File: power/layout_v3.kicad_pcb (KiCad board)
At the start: 2 copper layers, 38.1 x 58.4 mm, 11 parts

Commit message: Minor changes after first combine
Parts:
- removed REF** (x2): PinHeader_1x20_P2.54mm_Vertical, Connector_PinHeader_2.54mm:PinHeader_1x20_P2.54mm_Vertical
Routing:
- net VDD: track 62.3 -> 70.4 mm
- net +5V: track 33.3 -> 37.3 mm
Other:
- board outline removed

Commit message: WIP STM32{F,L}xxxCxTx layout
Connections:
- net +5V renamed 5V
- PD3 pad 2: (no net) -> VBAT
- PJ1 pad 4: (no net) -> Net-(PJ1-Pad4)
- PSJ1 pad 2: (no net) -> USB_D+
- PSJ2 pad 2: (no net) -> USB_D-
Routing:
- net +5V: track 0.00 -> 31.2 mm
- net 5V: track 37.3 -> 6.10 mm
- net VBAT: track 0.00 -> 16.3 mm
- net (no net): track 16.3 -> 0.00 mm
- net Net-(PJ1-Pad4): track 0.00 -> 11.5 mm
- net Net-(PJ1-Pad2): track 5.99 -> 5.27 mm
- net Net-(PJ1-Pad3): track 4.56 -> 5.27 mm
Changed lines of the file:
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@@
     (thickness 1.6)
     (drawings 16)
-    (tracks 56)
+    (tracks 61)
     (zones 0)
     (modules 9)
-    (nets 8)
+    (nets 13)
   )
   (page A4)
@@
   (net 6 "Net-(PJ1-Pad2)")
   (net 7 +5V)
+  (net 8 5V)
+  (net 9 VBAT)
+  (net 10 "Net-(PJ1-Pad4)")
+  (net 11 USB_D+)
+  (net 12 USB_D-)
   (net_class Default "Dit is de standaard class."
     (clearance 0.2)
@@
     (uvia_drill 0.1)
     (add_net +5V)
+    (add_net 5V)
     (add_net GND)
     (add_net "Net-(PJ1-Pad2)")
     (add_net "Net-(PJ1-Pad3)")
+    (add_net "Net-(PJ1-Pad4)")
+    (add_net USB_D+)
+    (add_net USB_D-)
+    (add_net VBAT)
     (add_net VBUS)
     (add_net VDD)
@@
       ))
     (pad 2 smd custom (at 0.65 0 270) (size 1 0.5) (layers B.Cu B.Mask)
-      (zone_connect 2)
+      (net 12 USB_D-) (zone_connect 2)
       (options (clearance outline) (anchor rect))
       (primitives
@@
       ))
     (pad 2 smd custom (at 0.65 0 270) (size 1 0.5) (layers B.Cu B.Mask)
-      (zone_connect 2)
+      (net 11 USB_D+) (zone_connect 2)
       (options (clearance outline) (anchor rect))
       (primitives
@@
     (pad 5 smd rect (at 1.3 -1.9 180) (size 0.45 1.3) (layers F.Cu F.Paste F.Mask)
       (net 1 GND))
-    (pad 4 smd rect (at 0.65 -1.9 180) (size 0.45 1.3) (layers F.Cu F.Paste F.Mask))
+    (pad 4 smd rect (at 0.65 -1.9 180) (size 0.45 1.3) (layers F.Cu F.Paste F.Mask)
+      (net 10 "Net-(PJ1-Pad4)"))
     (pad 3 smd rect (at 0 -1.9 180) (size 0.45 1.3) (layers F.Cu F.Paste F.Mask)
       (net 5 "Net-(PJ1-Pad3)"))
@@
     (fp_line (start -0.7 -0.6) (end -1 -0.3) (layer F.Fab) (width 0.1))
     (fp_line (start 1 -0.6) (end -0.7 -0.6) (layer F.Fab) (width 0.1))
-    (pad 2 smd roundrect (at 1.025 0) (size 1.15 1.4) (layers F.Cu F.Paste F.Mask) (roundrect_rratio 0.217391))
+    (pad 2 smd roundrect (at 1.025 0) (size 1.15 1.4) (layers F.Cu F.Paste F.Mask) (roundrect_rratio 0.217391)
+      (net 9 VBAT))
     (pad 1 smd roundrect (at -1.025 0) (size 1.15 1.4) (layers F.Cu F.Paste F.Mask) (roundrect_rratio 0.217391)
       (net 2 VREG_IN))
@@
       (net 4 VBUS))
     (pad 1 smd roundrect (at -1.025 0) (size 1.15 1.4) (layers F.Cu F.Paste F.Mask) (roundrect_rratio 0.217391)
-      (net 7 +5V))
+      (net 8 5V))
     (model ${KISYS3DMOD}/Diode_SMD.3dshapes/D_0805_2012Metric.wrl
       (at (xyz 0 0 0))
@@
   (gr_line (start 132.08 109.22) (end 170.18 109.22) (layer Dwgs.User) (width 0.05))
   (gr_line (start 132.08 50.8) (end 132.08 109.22) (layer Dwgs.User) (width 0.05))
-  (segment (start 162.56 60.96) (end 162.56 63.5) (width 0.25) (layer F.Cu) (net 0))
-  (segment (start 150.64 63.5) (end 149.37 62.23) (width 0.25) (layer F.Cu) (net 0))
-  (segment (start 162.56 63.5) (end 150.64 63.5) (width 0.25) (layer F.Cu) (net 0))
+  (segment (start 162.56 60.96) (end 162.56 63.5) (width 0.25) (layer F.Cu) (net 9))
+  (segment (start 150.64 63.5) (end 149.37 62.23) (width 0.25) (layer F.Cu) (net 9))
+  (segment (start 162.56 63.5) (end 150.64 63.5) (width 0.25) (layer F.Cu) (net 9))
   (via (at 143.256 70.104) (size 0.8) (drill 0.4) (layers F.Cu B.Cu) (net 1))
   (segment (start 145.025 69.85) (end 143.51 69.85) (width 0.25) (layer F.Cu) (net 1))
@@
   (segment (start 146.08 60.93) (end 146.08 56.51) (width 0.25) (layer F.Cu) (net 4))
   (segment (start 144.78 62.23) (end 146.08 60.93) (width 0.25) (layer F.Cu) (net 4))
-  (via (at 143.51 58.42) (size 0.8) (drill 0.4) (layers F.Cu B.Cu) (net 5))
-  (segment (start 142.24 59.69) (end 143.51 58.42) (width 0.25) (layer B.Cu) (net 5))
-  (segment (start 144.78 57.41) (end 144.78 56.51) (width 0.25) (layer F.Cu) (net 5))
-  (segment (start 144.075685 58.42) (end 144.78 57.715685) (width 0.25) (layer F.Cu) (net 5))
-  (segment (start 144.78 57.715685) (end 144.78 57.41) (width 0.25) (layer F.Cu) (net 5))
-  (segment (start 143.51 58.42) (end 144.075685 58.42) (width 0.25) (layer F.Cu) (net 5))
-  (via (at 144.78 59.69) (size 0.8) (drill 0.4) (layers F.Cu B.Cu) (net 6))
-  (segment (start 145.43 56.51) (end 145.43 59.04) (width 0.25) (layer F.Cu) (net 6))
-  (segment (start 145.43 59.04) (end 144.78 59.69) (width 0.25) (layer F.Cu) (net 6))
-  (segment (start 144.78 59.69) (end 147.32 59.69) (width 0.25) (layer B.Cu) (net 6))
-  (segment (start 141.46 60.96) (end 142.73 62.23) (width 0.25) (layer F.Cu) (net 7))
-  (segment (start 139.7 60.96) (end 141.46 60.96) (width 0.25) (layer F.Cu) (net 7))
-  (segment (start 139.7 60.96) (end 139.7 63.5) (width 0.25) (layer F.Cu) (net 7))
+  (via (at 144.018 59.69) (size 0.8) (drill 0.4) (layers F.Cu B.Cu) (net 5))
+  (segment (start 144.018 58.477685) (end 144.018 59.69) (width 0.25) (layer F.Cu) (net 5))
+  (segment (start 144.78 56.51) (end 144.78 57.715685) (width 0.25) (layer F.Cu) (net 5))
+  (segment (start 144.78 57.715685) (end 144.018 58.477685) (width 0.25) (layer F.Cu) (net 5))
+  (segment (start 144.018 59.69) (end 142.24 59.69) (width 0.25) (layer B.Cu) (net 5))
+  (via (at 145.288 59.69) (size 0.8) (drill 0.4) (layers F.Cu B.Cu) (net 6))
+  (segment (start 147.32 59.69) (end 145.288 59.69) (width 0.25) (layer B.Cu) (net 6))
+  (segment (start 145.43 59.548) (end 145.288 59.69) (width 0.25) (layer F.Cu) (net 6))
+  (segment (start 145.43 56.51) (end 145.43 59.548) (width 0.25) (layer F.Cu) (net 6))
+  (segment (start 141.46 60.96) (end 142.73 62.23) (width 0.25) (layer F.Cu) (net 8))
+  (segment (start 139.7 60.96) (end 141.46 60.96) (width 0.25) (layer F.Cu) (net 8))
+  (segment (start 139.7 60.96) (end 139.7 63.5) (width 0.25) (layer F.Cu) (net 8))
   (segment (start 151.13 54.61) (end 154.305 51.435) (width 0.25) (layer B.Cu) (net 7))
   (segment (start 138.43 62.23) (end 136.525 62.23) (width 0.25) (layer B.Cu) (net 7))
@@
   (segment (start 135.89 54.864998) (end 136.144998 54.61) (width 0.25) (layer B.Cu) (net 7))
   (segment (start 136.144998 54.61) (end 151.13 54.61) (width 0.25) (layer B.Cu) (net 7))
+  (segment (start 144.13 57.41) (end 143.12 58.42) (width 0.25) (layer F.Cu) (net 10))
+  (segment (start 144.13 56.51) (end 144.13 57.41) (width 0.25) (layer F.Cu) (net 10))
+  (segment (start 143.12 58.42) (end 139.7 58.42) (width 0.25) (layer F.Cu) (net 10))
+  (segment (start 139.7 58.42) (end 139.446 58.42) (width 0.25) (layer F.Cu) (net 10))
+  (segment (start 139.446 58.42) (end 138.43 59.436) (width 0.25) (layer F.Cu) (net 10))
+  (segment (start 138.43 59.436) (end 138.43 63.5) (width 0.25) (layer F.Cu) (net 10))
 )

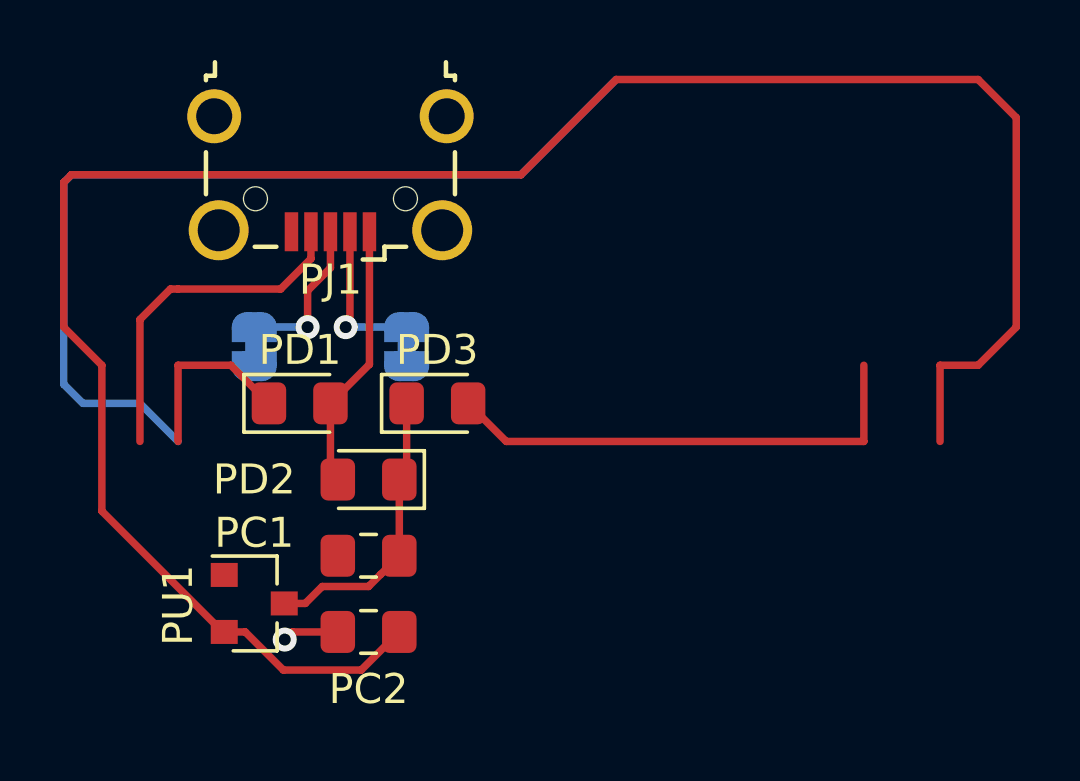
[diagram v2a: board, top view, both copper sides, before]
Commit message: Defining areas and connections per 'module'
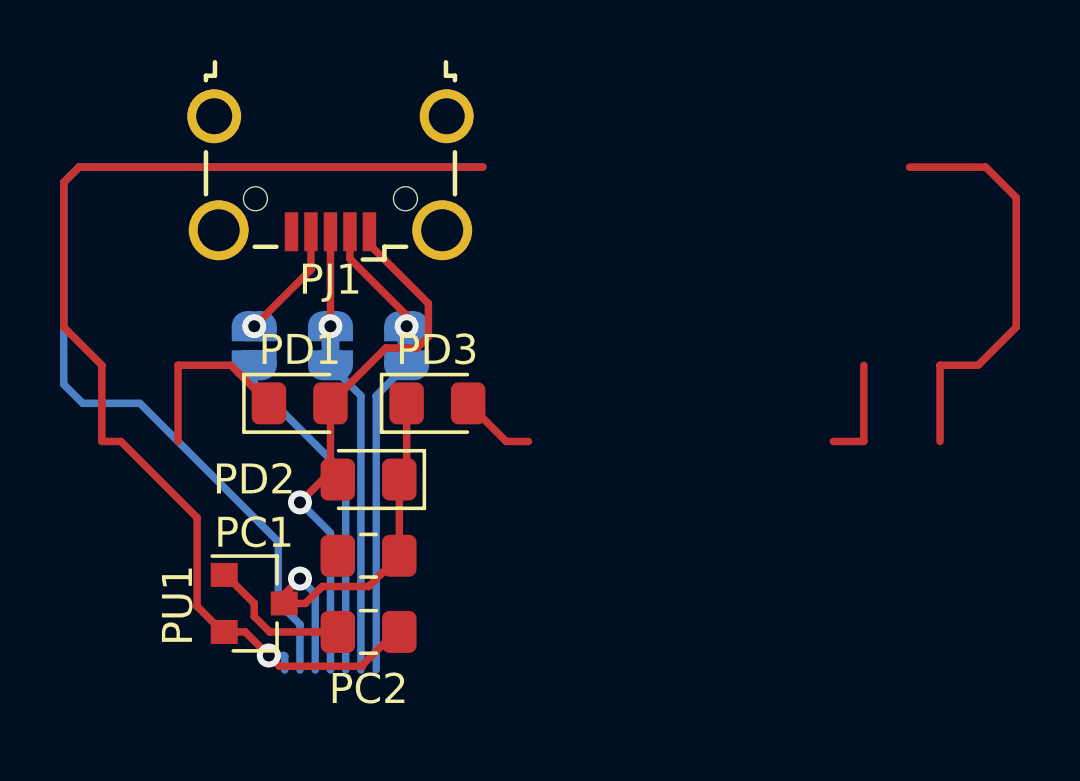
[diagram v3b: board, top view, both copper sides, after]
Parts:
- added PSJ3: ID, Jumper:SolderJumper-2_P1.3mm_Open_RoundedPad1.0x1.5mm, B.Cu at (142.2, 60.3)
- moved PSJ1 2.54 mm to (144.8, 60.3)
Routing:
- net VDD: track 70.4 -> 53.6 mm, vias 0 -> 1
- net USB_ID: track 0.00 -> 11.4 mm
- net USB_D-: track 0.00 -> 10.6 mm
- net USB_D+: track 0.00 -> 10.6 mm
- net VBAT: track 16.3 -> 6.10 mm
- net VBUS: track 8.90 -> 18.7 mm, vias 0 -> 1
- net Net-(PJ1-Pad4): track 11.5 -> 3.93 mm, vias 0 -> 1
- net VREG_IN: track 9.68 -> 14.0 mm, vias 0 -> 1
- net +5V: track 31.2 -> 34.8 mm
- net GND: track 1.87 -> 4.83 mm, vias 1 -> 0
- net Net-(PJ1-Pad3): track 5.27 -> 3.15 mm
- net Net-(PJ1-Pad2): track 5.27 -> 3.93 mm

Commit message: Changes after combining
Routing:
- net GND: track 4.83 -> 13.1 mm
- net VREG_IN: track 14.0 -> 15.5 mm
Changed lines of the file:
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@@
     (thickness 1.6)
     (drawings 208)
-    (tracks 89)
+    (tracks 95)
     (zones 0)
     (modules 10)
@@
   (segment (start 142.24 69.335002) (end 142.754998 69.85) (width 0.25) (layer F.Cu) (net 1))
   (segment (start 141.24 67.95) (end 141.29 67.95) (width 0.25) (layer F.Cu) (net 1))
+  (segment (start 141.105 56.51) (end 141.055 56.46) (width 0.25) (layer F.Cu) (net 1))
+  (segment (start 143.48 56.51) (end 141.105 56.51) (width 0.25) (layer F.Cu) (net 1))
+  (segment (start 145.025 69.85) (end 145.025 67.31) (width 0.25) (layer F.Cu) (net 1))
+  (segment (start 145.025 67.31) (end 146.295 68.58) (width 0.25) (layer F.Cu) (net 1))
+  (segment (start 146.295 68.58) (end 147.828 68.58) (width 0.25) (layer F.Cu) (net 1))
   (segment (start 147.32 64.525) (end 147.075 64.77) (width 0.25) (layer F.Cu) (net 2))
   (segment (start 147.32 62.23) (end 147.32 64.525) (width 0.25) (layer F.Cu) (net 2))
   (segment (start 147.075 64.77) (end 147.075 67.31) (width 0.25) (layer F.Cu) (net 2))
-  (segment (start 146.451628 67.933372) (end 147.075 67.31) (width 0.25) (layer F.Cu) (net 2))
-  (segment (start 146.04999 68.33501) (end 146.451628 67.933372) (width 0.25) (layer F.Cu) (net 2))
-  (segment (start 144.50499 68.33501) (end 146.04999 68.33501) (width 0.25) (layer F.Cu) (net 2))
-  (segment (start 143.94 68.9) (end 144.50499 68.33501) (width 0.25) (layer F.Cu) (net 2))
   (segment (start 143.24 68.9) (end 143.94 68.9) (width 0.25) (layer F.Cu) (net 2))
   (via (at 143.764 68.072) (size 0.8) (drill 0.4) (layers F.Cu B.Cu) (net 2))
@@
   (segment (start 143.764 68.072) (end 144.272 68.58) (width 0.25) (layer B.Cu) (net 2))
   (segment (start 144.272 68.58) (end 144.272 71.12) (width 0.25) (layer B.Cu) (net 2))
+  (segment (start 146.04999 65.79501) (end 146.451628 65.393372) (width 0.25) (layer F.Cu) (net 2))
+  (segment (start 144.9518 65.79501) (end 146.04999 65.79501) (width 0.25) (layer F.Cu) (net 2))
+  (segment (start 146.451628 65.393372) (end 147.075 64.77) (width 0.25) (layer F.Cu) (net 2))
+  (segment (start 143.764 66.98281) (end 144.9518 65.79501) (width 0.25) (layer F.Cu) (net 2))
+  (segment (start 143.764 68.072) (end 143.764 66.98281) (width 0.25) (layer F.Cu) (net 2))
   (segment (start 147.075 69.723) (end 145.805 70.993) (width 0.25) (layer F.Cu) (net 3))
   (segment (start 167.64 59.69) (end 166.37 60.96) (width 0.25) (layer F.Cu) (net 3))
